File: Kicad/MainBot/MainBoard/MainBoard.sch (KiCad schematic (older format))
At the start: 55 parts, among them J1 Conn_01x02, J10 Conn_01x24, J11 01x24, J12 Conn_01x05, J13 Conn_01x03, J14 Conn_01x03, J15 Conn_01x03, J16 Conn_01x04, J17 Conn_01x04, J18 Conn_01x04, J19 Conn_01x04, J20 Conn_01x03, U1 AZ1117-3.3, U2 TCA9548A, U3 Teensy3.6, U4 DRV8825, U5 DRV8825, U6 DRV8825, U7 DRV8825

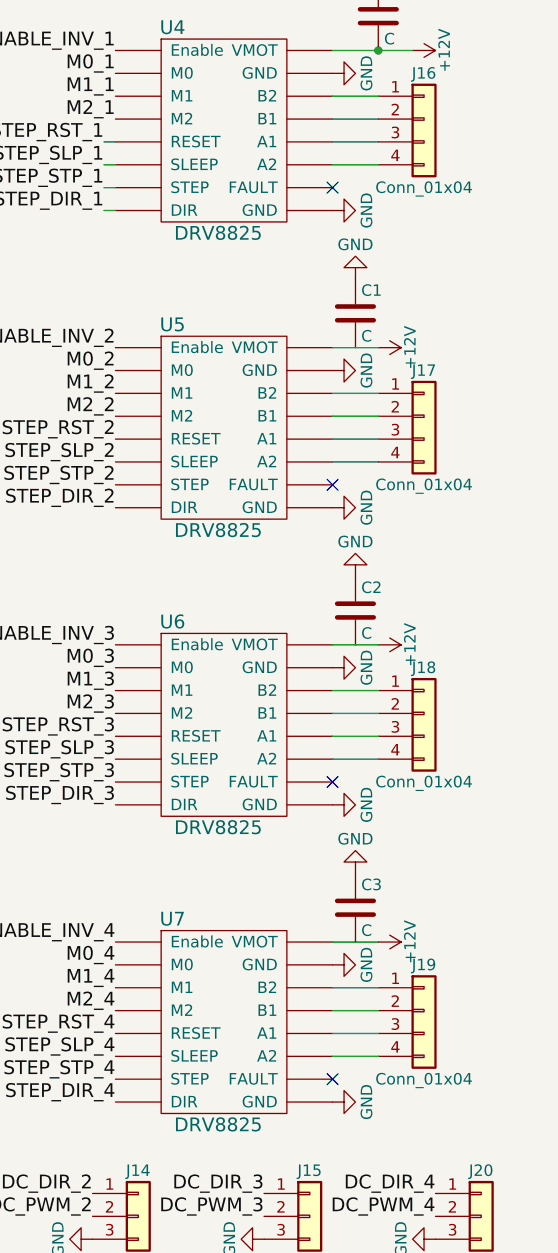
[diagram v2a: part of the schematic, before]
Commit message: Removed NC on FAULT pins of Step drivers
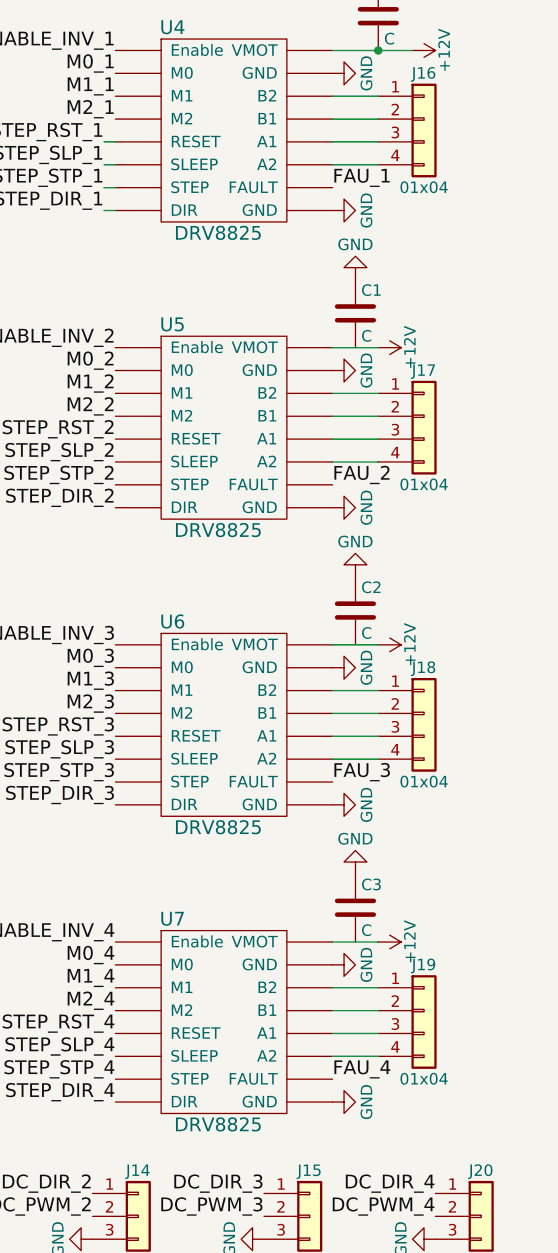
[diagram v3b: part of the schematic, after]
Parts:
- J16, J17, J18, J19: value Conn_01x04 -> 01x04
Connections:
- new net FAU_1: U4.~ (VMOT)
- new net FAU_2: U5.~ (VMOT)
- new net FAU_3: U6.~ (VMOT)
- new net FAU_4: U7.~ (VMOT)
- no-connect marks 7 -> 3
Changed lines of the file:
@@
 P 10700 1450
 F 0 "J16" H 10700 1650 50  0000 C CNN
-F 1 "Conn_01x04" H 10700 1150 50  0000 C CNN
+F 1 "01x04" H 10700 1150 50  0000 C CNN
 F 2 "Pin_Headers:Pin_Header_Straight_1x04_Pitch2.54mm" H 10700 1450 50  0001 C CNN
 F 3 "" H 10700 1450 50  0001 C CNN
@@
 	1    0    0    -1
 $EndComp
-NoConn ~ 10300 1750
 $Comp
 L GND #PWR015
@@
 P 10700 2750
 F 0 "J17" H 10700 2950 50  0000 C CNN
-F 1 "Conn_01x04" H 10700 2450 50  0000 C CNN
+F 1 "01x04" H 10700 2450 50  0000 C CNN
 F 2 "Pin_Headers:Pin_Header_Straight_1x04_Pitch2.54mm" H 10700 2750 50  0001 C CNN
 F 3 "" H 10700 2750 50  0001 C CNN
@@
 	1    0    0    -1
 $EndComp
-NoConn ~ 10300 3050
 $Comp
 L C C2
@@
 P 10700 4050
 F 0 "J18" H 10700 4250 50  0000 C CNN
-F 1 "Conn_01x04" H 10700 3750 50  0000 C CNN
+F 1 "01x04" H 10700 3750 50  0000 C CNN
 F 2 "Pin_Headers:Pin_Header_Straight_1x04_Pitch2.54mm" H 10700 4050 50  0001 C CNN
 F 3 "" H 10700 4050 50  0001 C CNN
@@
 	1    0    0    -1
 $EndComp
-NoConn ~ 10300 4350
 $Comp
 L GND #PWR024
@@
 P 10700 5350
 F 0 "J19" H 10700 5550 50  0000 C CNN
-F 1 "Conn_01x04" H 10700 5050 50  0000 C CNN
+F 1 "01x04" H 10700 5050 50  0000 C CNN
 F 2 "Pin_Headers:Pin_Header_Straight_1x04_Pitch2.54mm" H 10700 5350 50  0001 C CNN
 F 3 "" H 10700 5350 50  0001 C CNN
@@
 	1    0    0    -1
 $EndComp
-NoConn ~ 10300 5650
 $Comp
 L GND #PWR028
@@
 Text Label 9350 5350 2    60   ~ 0
 M2_4
+Text Label 10300 1750 0    60   ~ 0
+FAU_1
+Text Label 10300 3050 0    60   ~ 0
+FAU_2
+Text Label 10300 4350 0    60   ~ 0
+FAU_3
+Text Label 10300 5650 0    60   ~ 0
+FAU_4
 $EndSCHEMATC

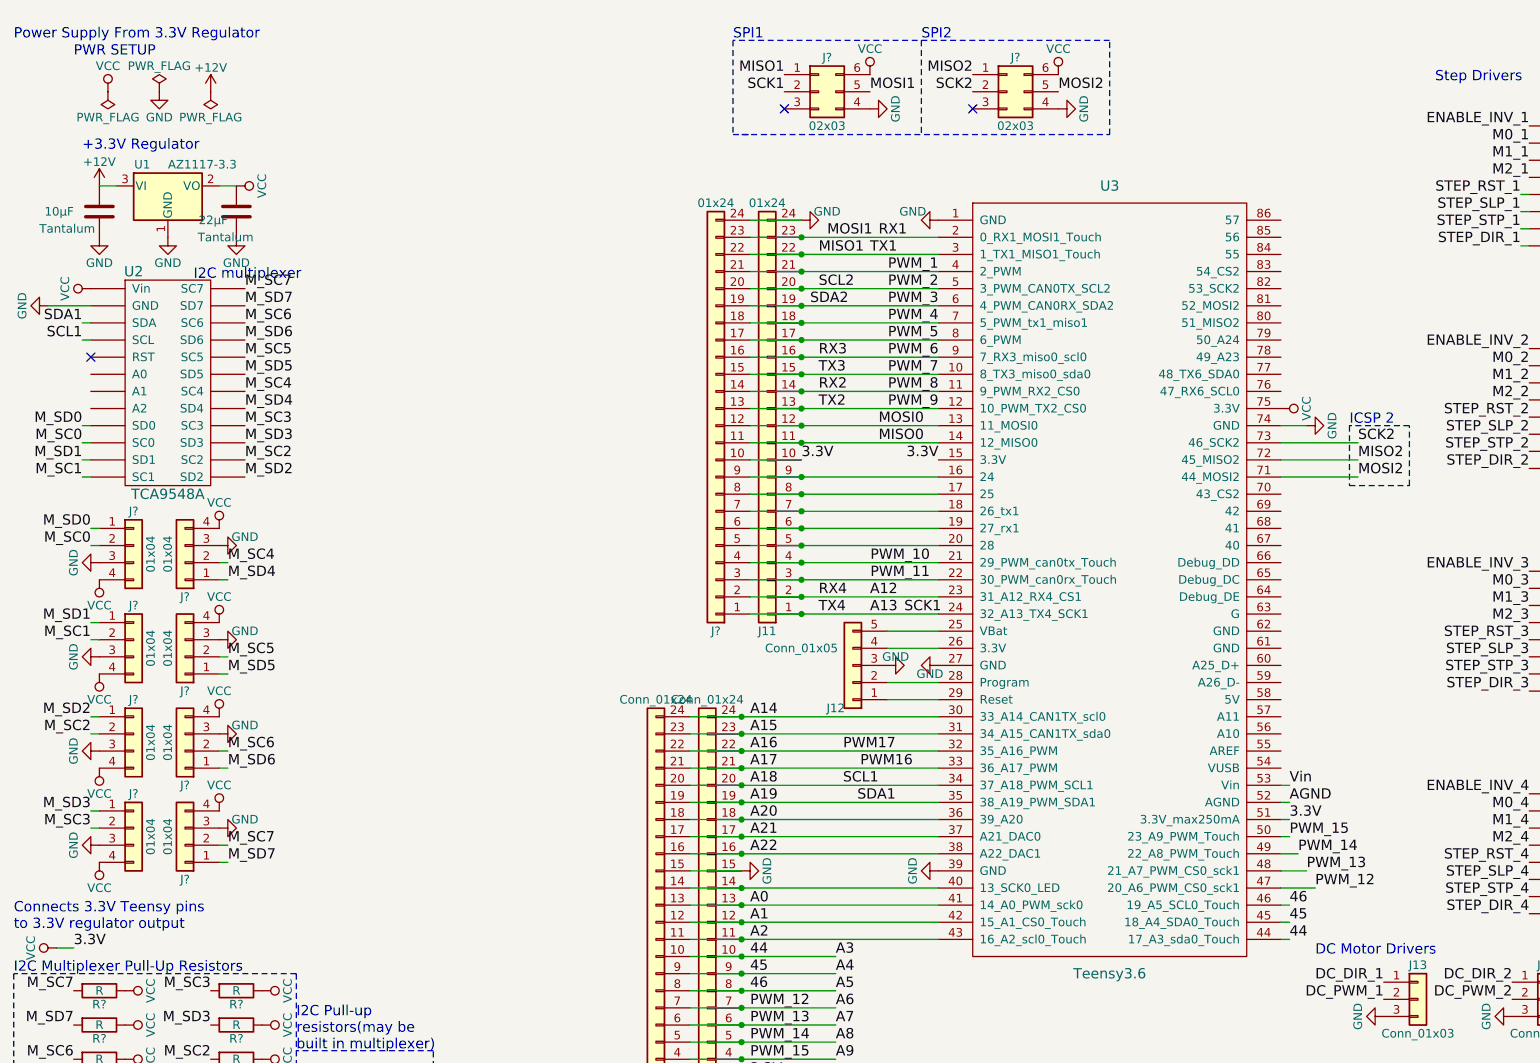
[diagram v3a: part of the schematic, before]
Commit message: Added Analog INs and OUTs
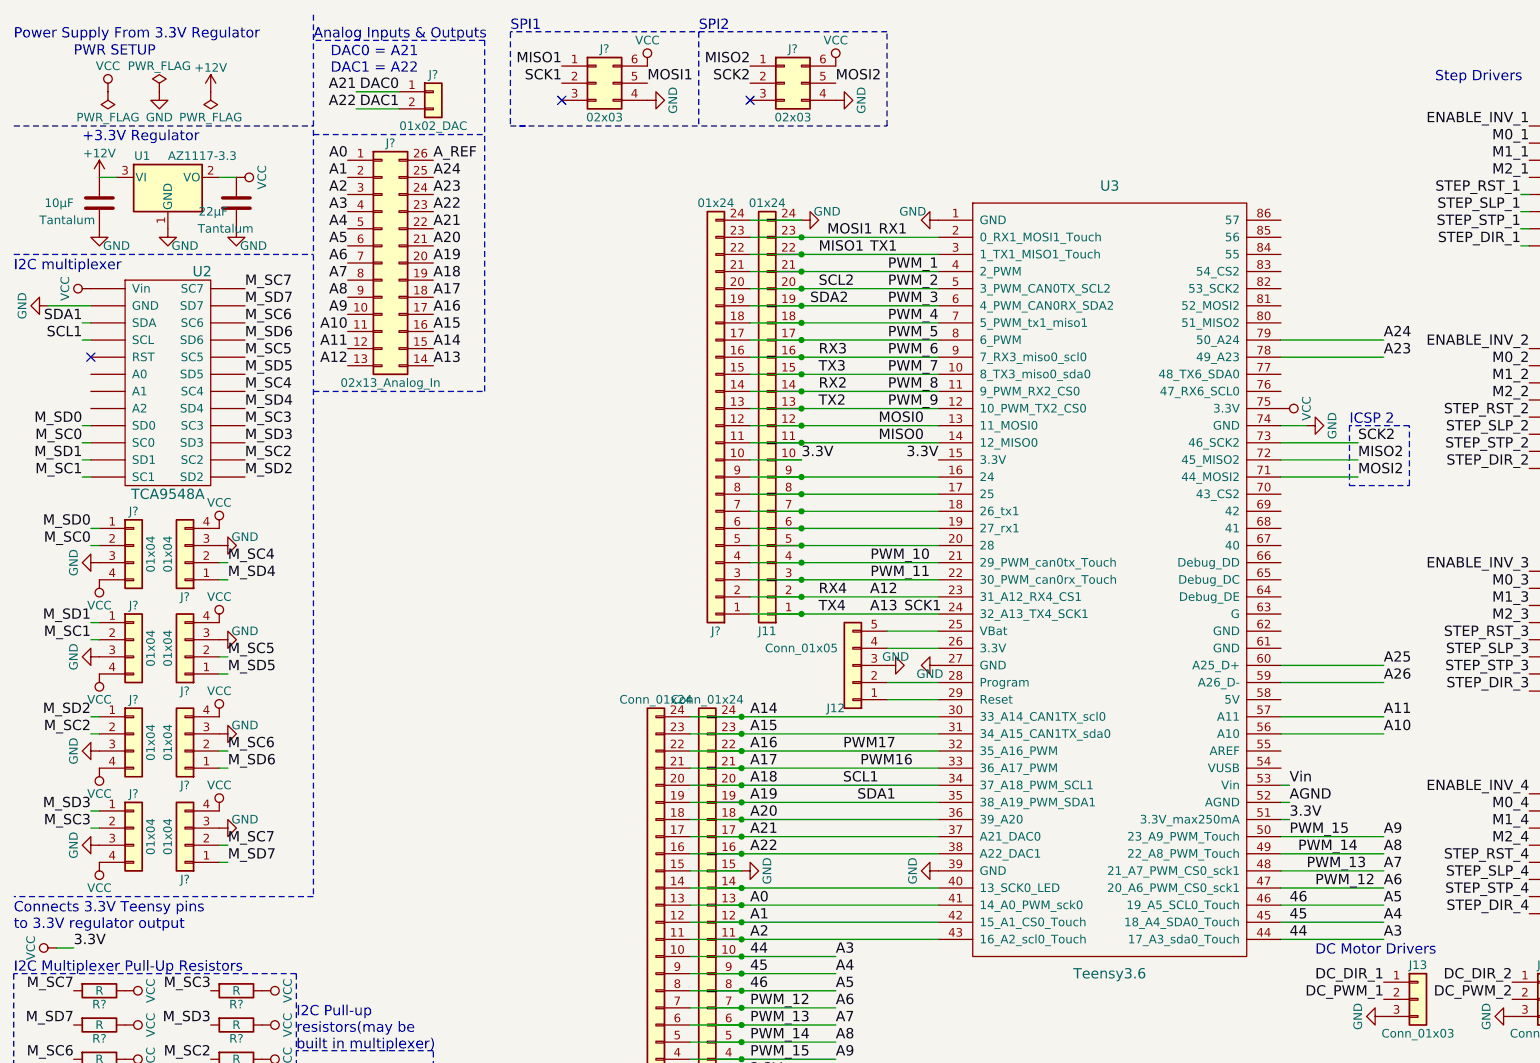
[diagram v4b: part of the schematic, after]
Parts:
- added J?: 02x13_Analog_In, symbol Conn_02x13_Counter_Clockwise
- added J?: 01x02_DAC, symbol Conn_01x02
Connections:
- net 44: now also J?.4 (Pin_4)
- net 45: now also J?.5 (Pin_5)
- net 46: now also J?.6 (Pin_6)
- net A0: now also J?.1 (Pin_1)
- net A1: now also J?.2 (Pin_2)
- net A12: now also J?.13 (Pin_13)
- net A13: now also J?.14 (Pin_14)
- net A14: now also J?.15 (Pin_15)
- net A15: now also J?.16 (Pin_16)
- net A16: now also J?.17 (Pin_17)
- net A17: now also J?.18 (Pin_18)
- net A18: now also J?.19 (Pin_19)
- net A19: now also J?.20 (Pin_20)
- net A2: now also J?.3 (Pin_3)
- net A20: now also J?.21 (Pin_21)
- net A21: now also J?.1 (Pin_1), J?.22 (Pin_22)
- net A22: now also J?.2 (Pin_2), J?.23 (Pin_23)
- net A6: now also J?.7 (Pin_7)
- net A7: now also J?.8 (Pin_8)
- net A8: now also J?.9 (Pin_9)
- net A9: now also J?.10 (Pin_10)
- net A10: now reaches U3.56 (A10)
- net A10: now also J?.11 (Pin_11)
- net A11: now reaches U3.57 (A11)
- net A11: now also J?.12 (Pin_12)
- net A26: now reaches U3.59 (A26_D-)
- net A25: now reaches U3.60 (A25_D+)
- net A23: now reaches U3.78 (49_A23)
- net A23: now also J?.24 (Pin_24)
- net A24: now reaches U3.79 (50_A24)
- net A24: now also J?.25 (Pin_25)
- new net A_REF: J?.26 (Pin_26)
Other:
- note added: "Analog Inputs & Outputs\n"
- note added: "DAC0 = A21\nDAC1 = A22\n"
- moved on the sheet: J?, Tantalum, U1

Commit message: Increased Schematic Size
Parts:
- added J?: 02x05_PWM, symbol Conn_02x05_Counter_Clockwise
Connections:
- net PWM_1: now also J?.1 (Pin_1)
- net PWM_10: now also J?.10 (Pin_10)
- net PWM_2: now also J?.2 (Pin_2)
- net PWM_3: now also J?.3 (Pin_3)
- net PWM_4: now also J?.4 (Pin_4)
- net PWM_5: now also J?.5 (Pin_5)
- net PWM_6: now also J?.6 (Pin_6)
- net PWM_7: now also J?.7 (Pin_7)
- net PWM_8: now also J?.8 (Pin_8)
- net PWM_9: now also J?.9 (Pin_9)
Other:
- note added: "(10)\n"
- note added: "(2)\n"
- note added: "(29)\n"
- note added: "(6)\n"
- note added: "(7)\n"
- note added: "I2C Pull-up\nresistors(10kR\nincluded in multiplexer)\n\n"
- note added: "PWM\n"
- note removed: "I2C Pull-up\nresistors(may be \nbuilt in multiplexer)\n\n"
- moved on the sheet: C1, C2, C3, C4, J1, J10, J11, J12, J13, J14, J15, J16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

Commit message: ?3
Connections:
- new net ADDR_0: U2.~ (Vin)
- new net ADDR_1: U2.~ (Vin)
- new net ADDR_2: U2.~ (Vin)
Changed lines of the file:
@@
 Wire Notes Line
 	1600 6850 500  6850
+Text Label 950  2600 2    60   ~ 0
+ADDR_0
+Text Label 950  2700 2    60   ~ 0
+ADDR_1
+Text Label 950  2800 2    60   ~ 0
+ADDR_2
 $EndSCHEMATC

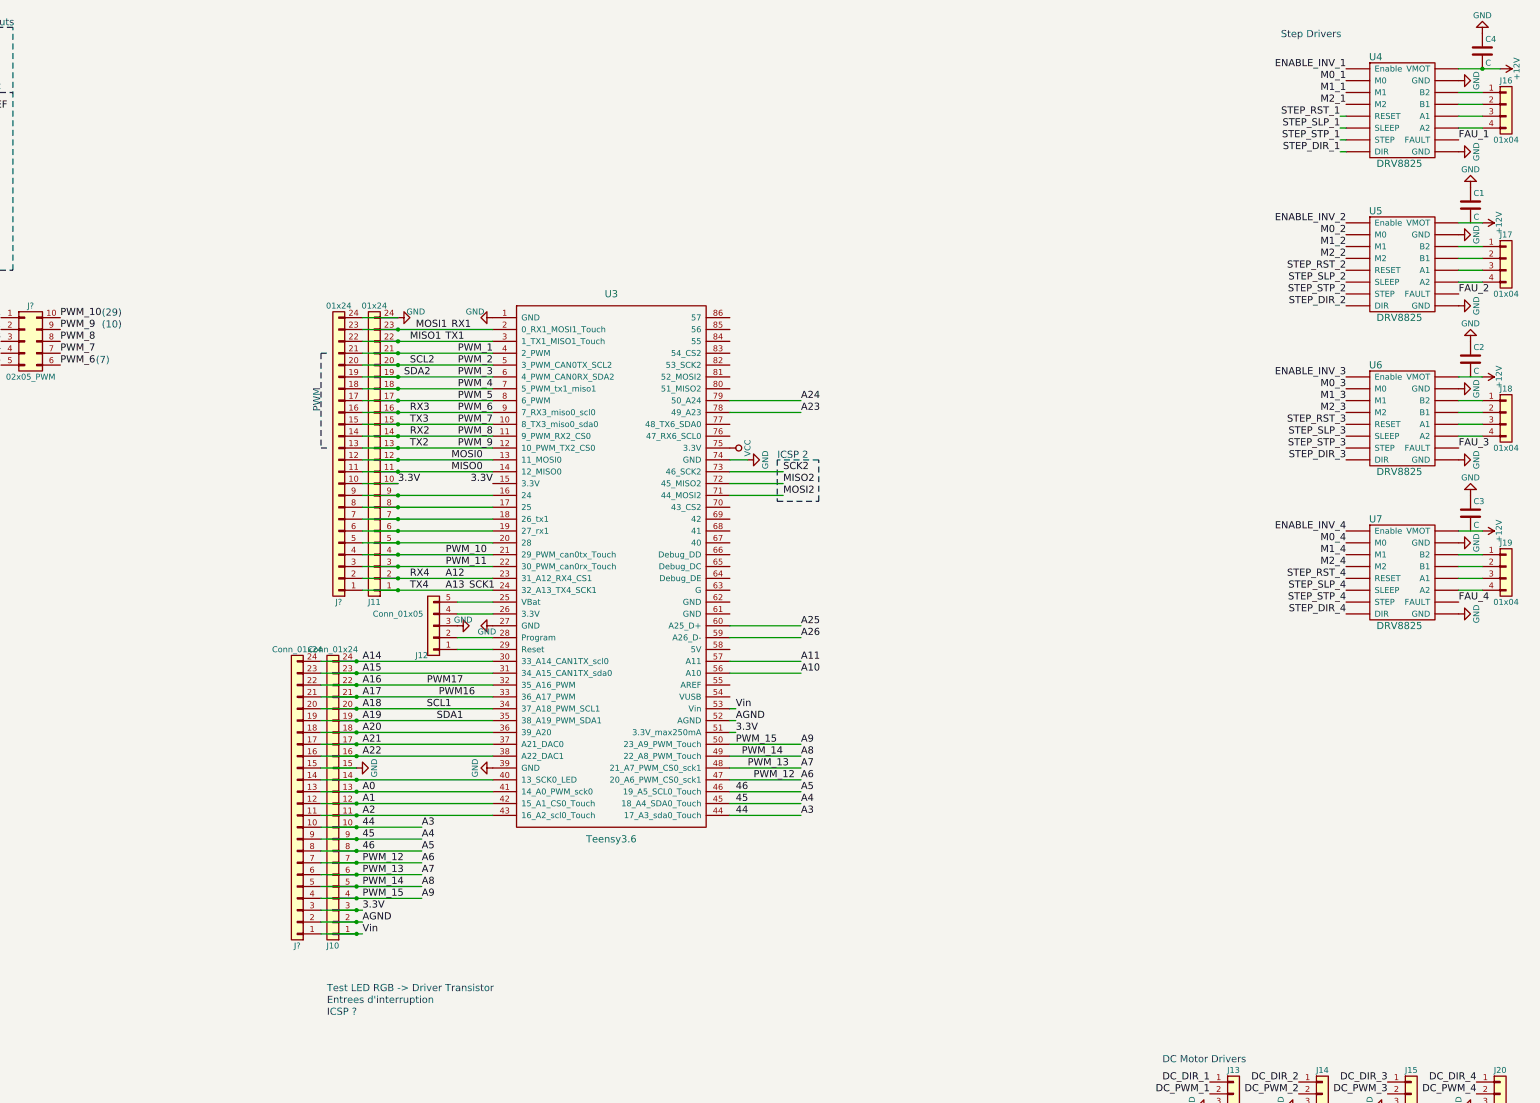
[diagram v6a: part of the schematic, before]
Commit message: Added stepper drivers' capacitors values
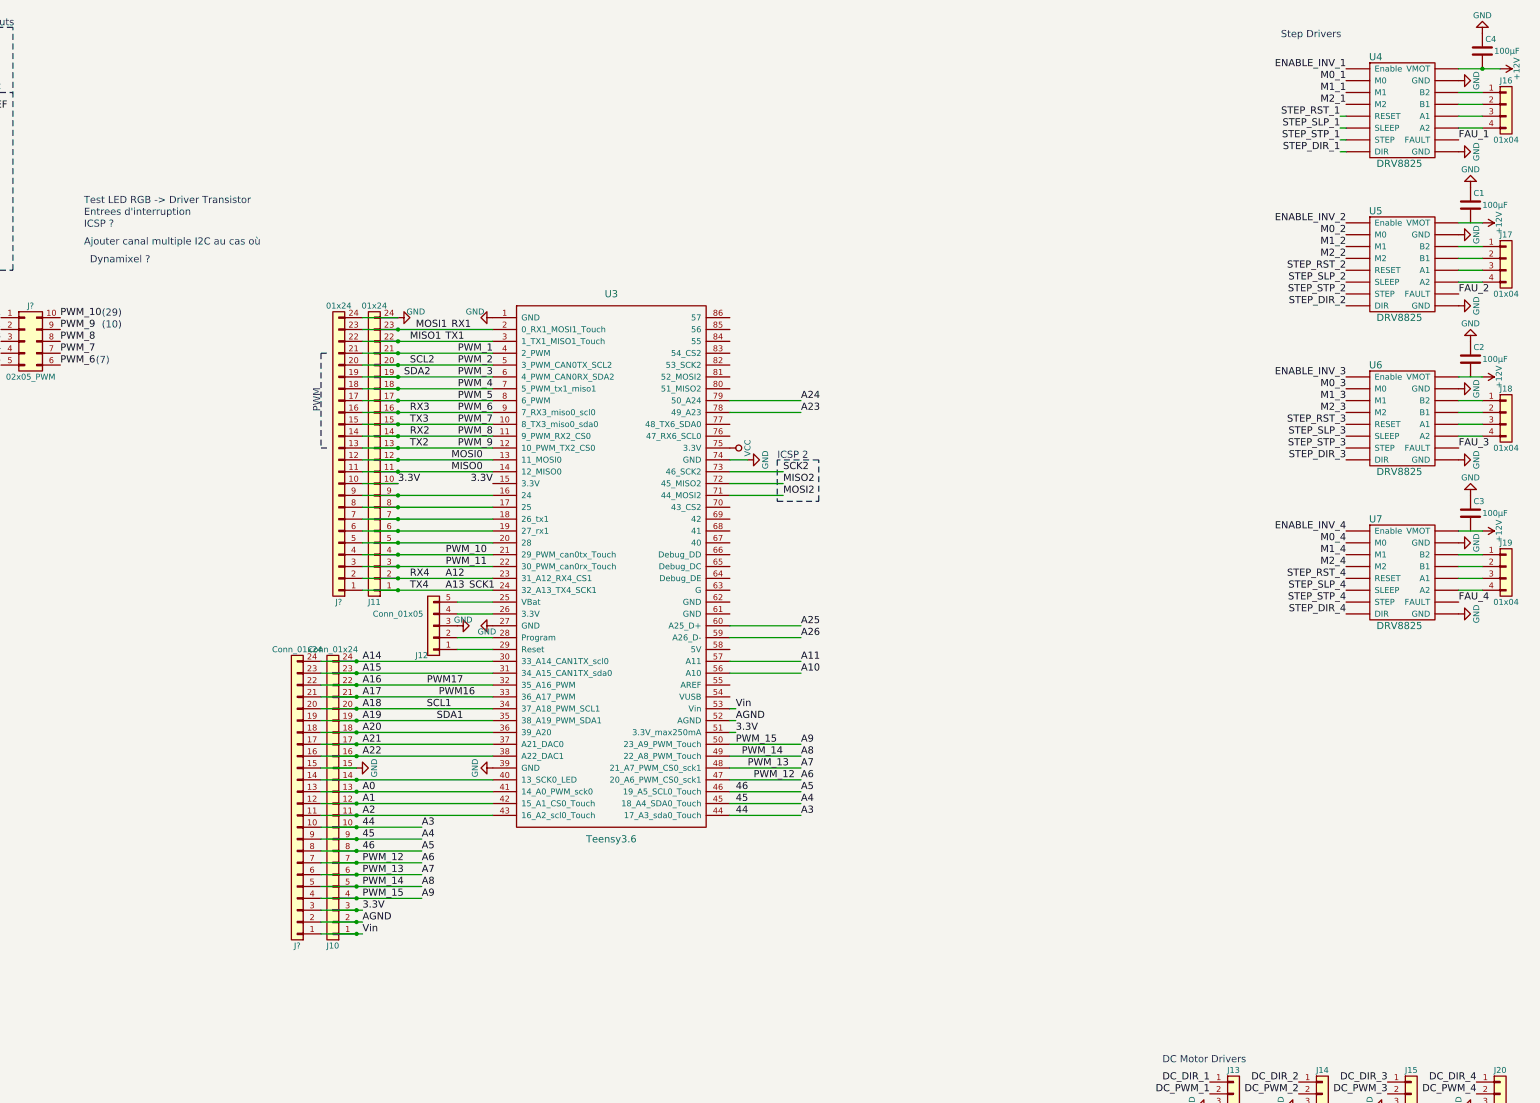
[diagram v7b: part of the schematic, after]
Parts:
- C1, C2, C3, C4: value C -> 100µF
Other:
- note added: "Ajouter canal multiple I2C au cas où\n"
- note added: "Dynamixel ?\n"
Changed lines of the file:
@@
 P 15650 850
 F 0 "C4" H 15675 950 50  0000 L CNN
-F 1 "C" H 15675 750 50  0000 L CNN
+F 1 "100µF" H 15750 850 50  0000 L CNN
 F 2 "Capacitors_THT:C_Disc_D4.7mm_W2.5mm_P5.00mm" H 15688 700 50  0001 C CNN
 F 3 "" H 15650 850 50  0001 C CNN
@@
 P 15550 2150
 F 0 "C1" H 15575 2250 50  0000 L CNN
-F 1 "C" H 15575 2050 50  0000 L CNN
+F 1 "100µF" H 15650 2150 50  0000 L CNN
 F 2 "Capacitors_THT:C_Disc_D4.7mm_W2.5mm_P5.00mm" H 15588 2000 50  0001 C CNN
 F 3 "" H 15550 2150 50  0001 C CNN
@@
 P 15550 3450
 F 0 "C2" H 15575 3550 50  0000 L CNN
-F 1 "C" H 15575 3350 50  0000 L CNN
+F 1 "100µF" H 15650 3450 50  0000 L CNN
 F 2 "Capacitors_THT:C_Disc_D4.7mm_W2.5mm_P5.00mm" H 15588 3300 50  0001 C CNN
 F 3 "" H 15550 3450 50  0001 C CNN
@@
 P 15550 4750
 F 0 "C3" H 15575 4850 50  0000 L CNN
-F 1 "C" H 15575 4650 50  0000 L CNN
+F 1 "100µF" H 15650 4750 50  0000 L CNN
 F 2 "Capacitors_THT:C_Disc_D4.7mm_W2.5mm_P5.00mm" H 15588 4600 50  0001 C CNN
 F 3 "" H 15550 4750 50  0001 C CNN
@@
 Text Label 850  9400 0    60   ~ 0
 3.3V
-Text Notes 5900 8900 0    60   ~ 0
+Text Notes 3850 2250 0    60   ~ 0
 Entrees d'interruption\n
-Text Notes 5900 9000 0    60   ~ 0
+Text Notes 3850 2350 0    60   ~ 0
 ICSP ?\n
-Text Notes 5900 8800 0    60   ~ 0
+Text Notes 3850 2150 0    60   ~ 0
 Test LED RGB -> Driver Transistor\n
 $Comp
@@
 Text Label 950  2800 2    60   ~ 0
 ADDR_2
+Text Notes 3850 2500 0    60   ~ 0
+Ajouter canal multiple I2C au cas où\n
+Text Notes 3900 2650 0    60   ~ 0
+Dynamixel ?\n
 $EndSCHEMATC
